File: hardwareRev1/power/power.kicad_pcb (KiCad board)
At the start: 2 copper layers, 25 parts, among them IC1 ATTINY24A-M-FIXED, P1 VIN, P2 CONN_11X2, P3 AVRProg, U1 TPS63020, U2 NCP508

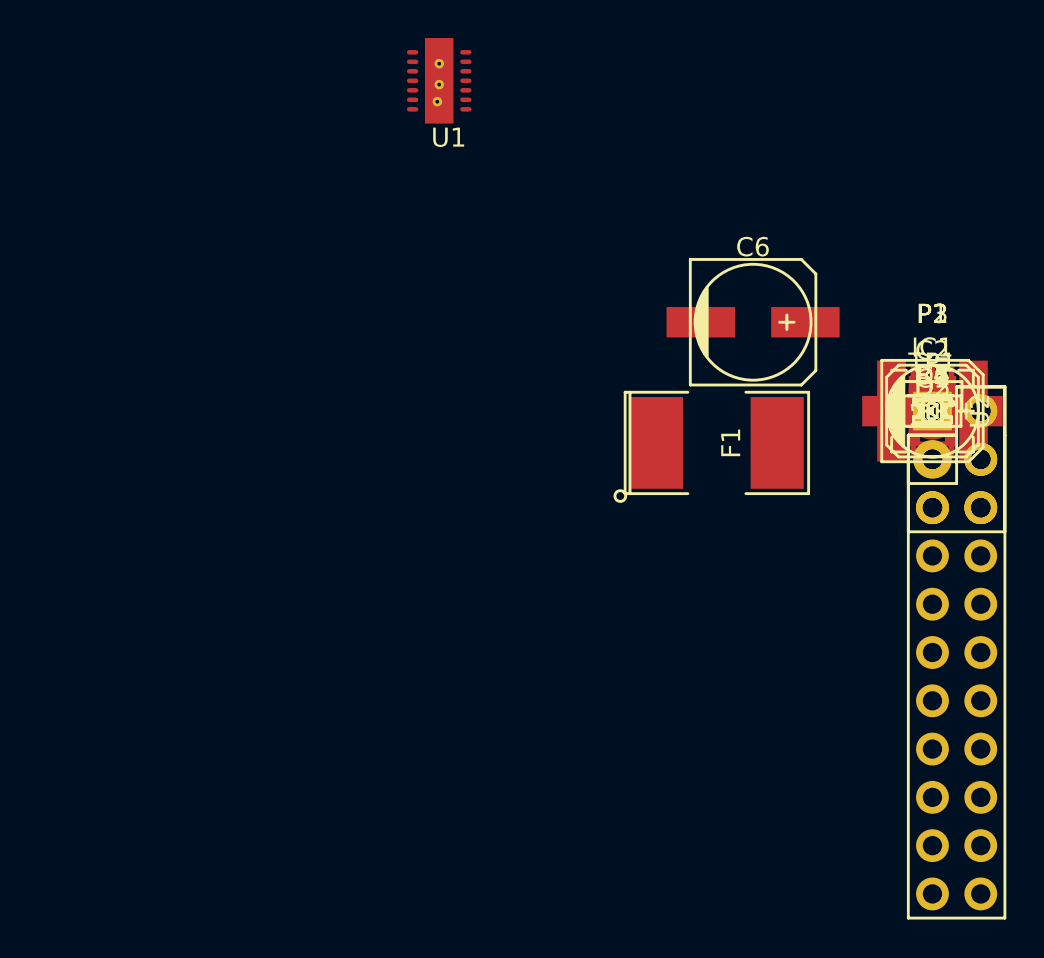
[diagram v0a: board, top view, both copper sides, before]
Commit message: Finished the power supbsystem.
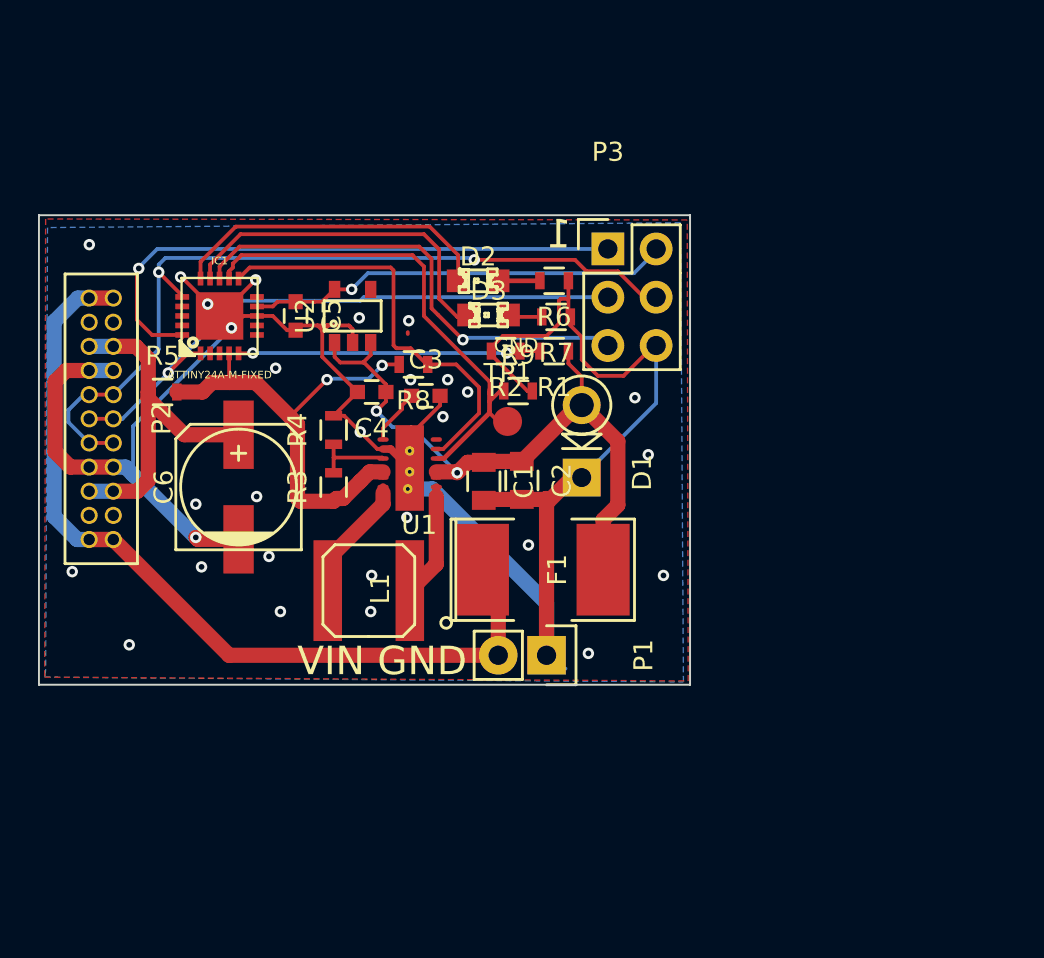
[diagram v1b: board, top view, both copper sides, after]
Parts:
- added G***: LOGO, hardwareRev1:giant, B.Cu at (122.8, 108.3)
- added R8: 100K, Resistors_SMD:R_0603, F.Cu at (121.2, 102.5)
- added R9: 100K, Resistors_SMD:R_0603, F.Cu at (126.7, 104.0)
- C1: footprint Capacitors_SMD:C_0201 -> Capacitors_SMD:C_0805
- C2: footprint Capacitors_SMD:c_elec_5x5.8 -> Capacitors_SMD:C_0805
- D1: footprint Diodes_SMD:SOD-323 -> Diodes_ThroughHole:Diode_DO-41_SOD81_Vertical_KathodeUp
- IC1: footprint Housings_DFN_QFN:QFN-20-1EP_4x4mm_Pitch0.5mm -> w_smd_qfn:qfn-20
- P2: footprint Pin_Headers:Pin_Header_Straight_2x11 -> hardwareRev1:1.27mmPitchHeader11X2
- R3: value 768J -> 768K
- R4: value 137J -> 137K
- R5: value R -> 0.01
- R6: value R -> 55
- TP1: value TEST-POINT2 -> EN; footprint Measurement_Points:Measurement_Point_Round-SMD-Pad_Big -> Measurement_Points:Measurement_Point_Round-SMD-Pad_Small
- U1: footprint TPS63020:TPS63020 -> hardwareRev1:TPS63020
- moved P2 43.1 mm to (105.4, 106.7)
- moved R5 40.5 mm to (108.0, 104.0)
- moved IC1 37.8 mm to (111.0, 100.0)
- moved C5 33.9 mm to (115.0, 100.0), turned to 270 degrees
- moved R3 31.8 mm to (117.0, 109.0), turned to 90 degrees
- moved R4 31.5 mm to (117.0, 106.0), turned to 90 degrees
- moved L1 31.1 mm to (118.8, 114.5), turned to 180 degrees
- moved U2 30.9 mm to (118.0, 100.0), turned to 180 degrees
- moved C4 29.5 mm to (119.0, 104.0), turned to 180 degrees
- moved C6 28.4 mm to (112.0, 109.0), turned to 90 degrees
- moved C3 26.7 mm to (121.8, 104.2)
- moved D2 24.9 mm to (124.6, 98.2)
- moved P1 24.0 mm to (128.2, 117.8), turned to 270 degrees
- moved D3 23.9 mm to (125.2, 100.0)
- moved C1 23.9 mm to (124.9, 108.7), turned to 270 degrees
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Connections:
- F1 pad 1: Net-(F1-Pad1) -> /BattIn
- IC1 pad 11: (no net) -> /PSave
- IC1 pad 2: (no net) -> Net-(IC1-Pad2)
- IC1 pad 3: +3.3V -> /ISenceHi
- L1 pad 1: (no net) -> Net-(L1-Pad1)
- L1 pad 2: (no net) -> Net-(L1-Pad2)
- P1 pad 2: Net-(F1-Pad1) -> /BattIn
- P2 pad 1: /Vin -> /BattIn
- P2 pad 19: /VOut2 -> Net-(P2-Pad19)
- P2 pad 2: /Vin -> /BattIn
- P2 pad 20: /VOut2 -> Net-(P2-Pad20)
- P2 pad 21: /Vin -> /BattIn
- P2 pad 22: /Vin -> /BattIn
- P2 pad 3: /VOut2 -> Net-(P2-Pad3)
- P2 pad 4: /VOut2 -> Net-(P2-Pad4)
- R7 pad 1: (no net) -> GND
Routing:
- net GND: track 0.00 -> 115.4 mm, vias 0 -> 26
- net /BattIn: track 0.00 -> 46.4 mm
- net /SDA: track 0.00 -> 43.2 mm, vias 0 -> 2
- net /Vin: track 0.00 -> 35.1 mm, vias 0 -> 2
- net /CLK: track 0.00 -> 32.2 mm, vias 0 -> 1
- net Net-(IC1-Pad20): track 0.00 -> 30.7 mm, vias 0 -> 1
- net /Enable: track 0.00 -> 26.5 mm
- net /ISense: track 0.00 -> 26.1 mm, vias 0 -> 2
- net Net-(IC1-Pad13): track 0.00 -> 25.3 mm, vias 0 -> 1
- net Net-(C5-Pad1): track 0.00 -> 22.4 mm, vias 0 -> 1
- net /PSave: track 0.00 -> 22.2 mm
- net +3.3V: track 0.00 -> 19.0 mm
- net Net-(D3-Pad1): track 0.00 -> 18.4 mm
- net Net-(D2-Pad1): track 0.00 -> 17.2 mm
- net /VSense: track 0.00 -> 16.0 mm, vias 0 -> 2
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- added copper zone on B.Cu, net GND
- added copper zone on F.Cu, net GND
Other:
- board outline added: 34.2 x 24.7 mm
- net class Default: clearance 0.2 -> 0.1524
- net class HighCurrent added: clearance 0.1524, trace_width 0.8, via_dia 0.6, via_drill 0.4
- rule trace_clearance: 0.2 -> 0.1524
- rule trace_min: 0.2 -> 0.1524
- rule via_min_size: 0.4 -> 0.3302
- board text added: "1"
- board text added: "AB1TJ PowerGiant 3v3@3AOut 3v3-5Vin"
- board text added: "GIANT"
- board text added: "GND"
- board text added: "REV0.A"
- board text added: "VIN GND"
- board text added: "Vin X 3v3Out Gnd SDA CLK SDA Gnd 3v3Out X Vin"

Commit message: board is almost done. Commiting before I destroy all my work...
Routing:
- net GND: track 115.4 -> 117.5 mm, vias 26 -> 17
- net (no net): track 0.10 -> 0.27 mm, vias 3 -> 11
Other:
- board text removed: "GND"

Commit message: board is done. Onto the radio module
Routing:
- net GND: track 117.5 -> 127.2 mm, vias 17 -> 16
- net (no net): track 0.27 -> 0.51 mm, vias 11 -> 2
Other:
- board outline removed

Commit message: added the radio .
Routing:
- net GND: track 127.2 -> 119.3 mm, vias 16 -> 9
- net (no net): track 0.51 -> 8.34 mm, vias 2 -> 9

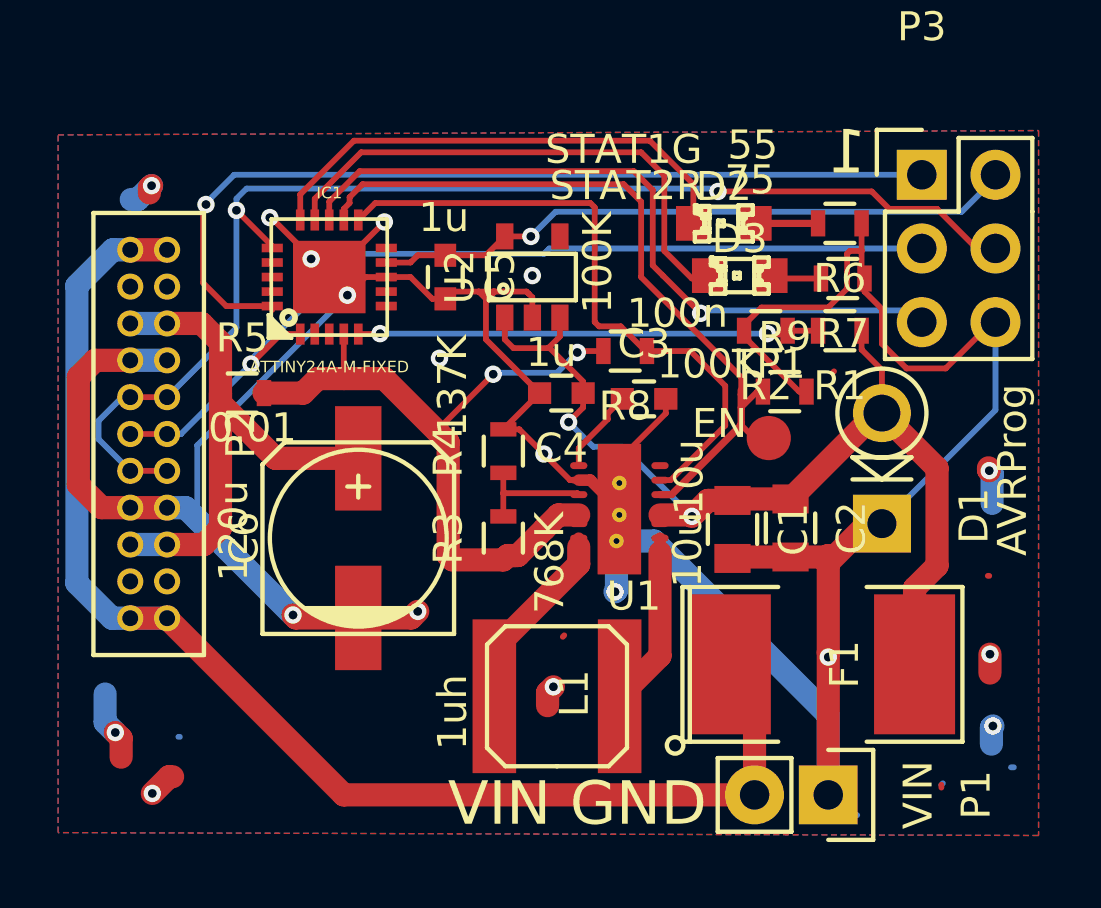
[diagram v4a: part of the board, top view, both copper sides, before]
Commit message: Fixed the errors with the initial layout
- Changed the pull resistor polarity on the enable pin.
- Brought the power save pull to Vin instead of Vout. I think this is
  better. Still defaults to non power saving
- Added more ground vias that will actually stay between zone fills.
- Made the current sensing actually work. Hi != High
Should work better.
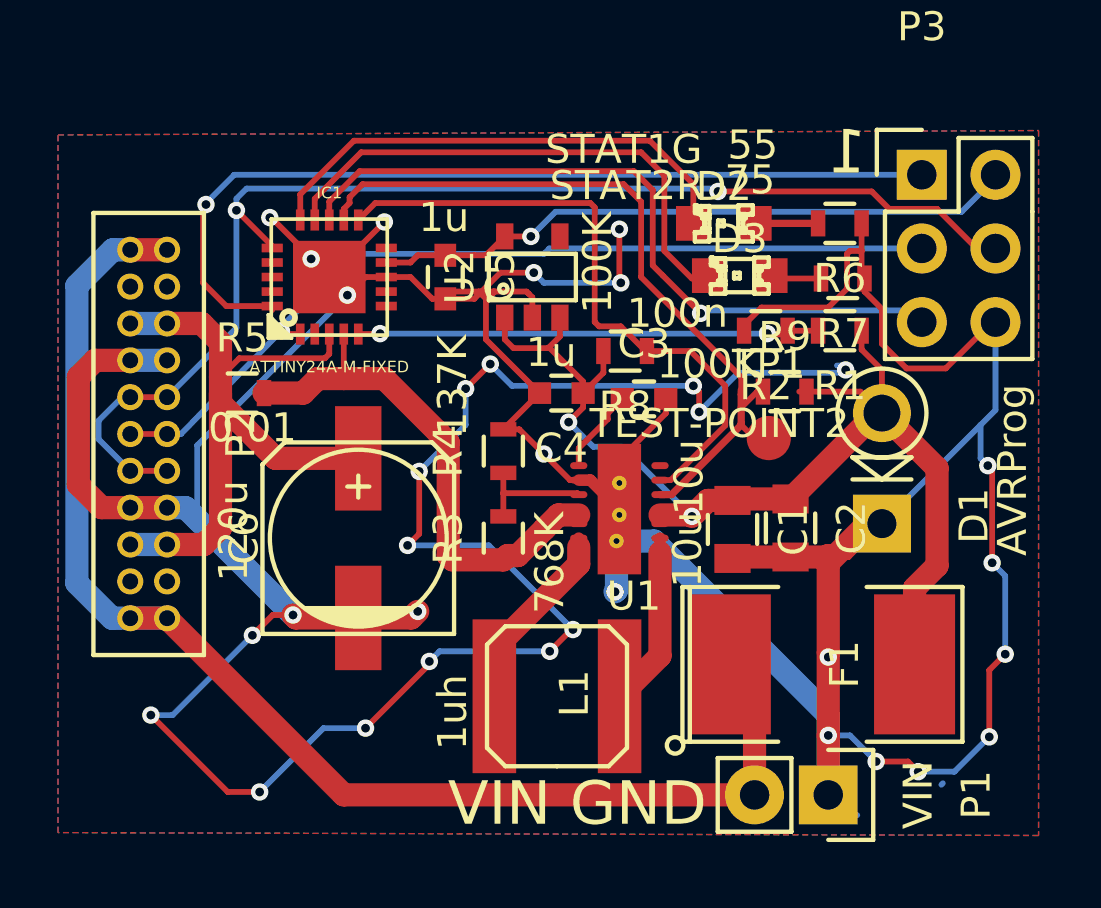
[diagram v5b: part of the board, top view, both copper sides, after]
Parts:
- TP1: value EN -> TEST-POINT2
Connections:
- IC1 pad 2: Net-(IC1-Pad2) -> (no net)
- IC1 pad 3: /ISenceHi -> +3.3V
- P2 pad 19: Net-(P2-Pad19) -> (no net)
- P2 pad 20: Net-(P2-Pad20) -> (no net)
- P2 pad 3: Net-(P2-Pad3) -> (no net)
- P2 pad 4: Net-(P2-Pad4) -> (no net)
- R8 pad 2: /ISense -> /Vin
- R9 pad 2: GND -> /Vin
- U1 pad 14: Net-(U1-Pad14) -> (no net)
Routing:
- net GND: track 119.3 -> 199.6 mm, vias 9 -> 33
- net (no net): track 8.34 -> 0.07 mm, vias 9 -> 0
- net /ISense: track 26.1 -> 19.0 mm, vias 2 -> 0
- net /Vin: track 35.1 -> 40.0 mm
- net +3.3V: track 19.0 -> 23.8 mm
- net /CLK: track 32.2 -> 30.8 mm
